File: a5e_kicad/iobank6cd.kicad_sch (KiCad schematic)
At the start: 1 part, among them U1 A5EB013B-B23B

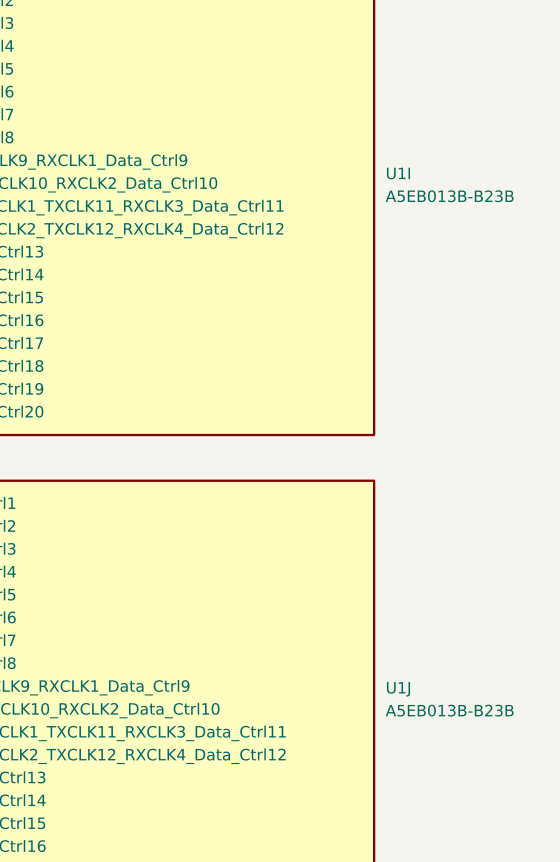
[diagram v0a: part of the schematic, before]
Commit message: add vias to lppdr balls
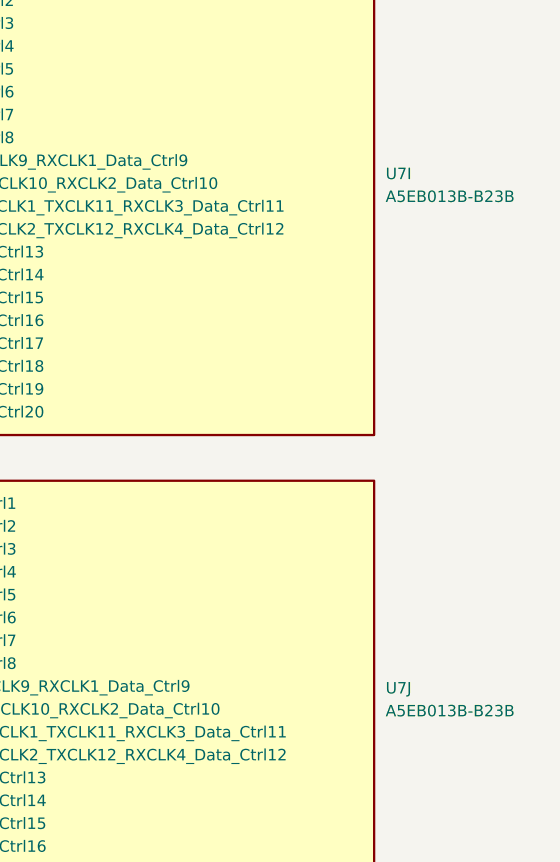
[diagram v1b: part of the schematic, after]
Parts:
- renumbered U1 to U7
